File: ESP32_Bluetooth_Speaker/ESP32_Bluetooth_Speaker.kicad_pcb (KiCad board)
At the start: 2 copper layers, 88.9 x 63.5 mm, 51 parts, among them J2 POWER INPUT, Q1 MMBT3904, Q2 MMBT3904, SW1 PAUSE, SW2 PREV, SW3 NEXT, SW4 V+, SW5 V-, SW6 RESET, U1 FT231XS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

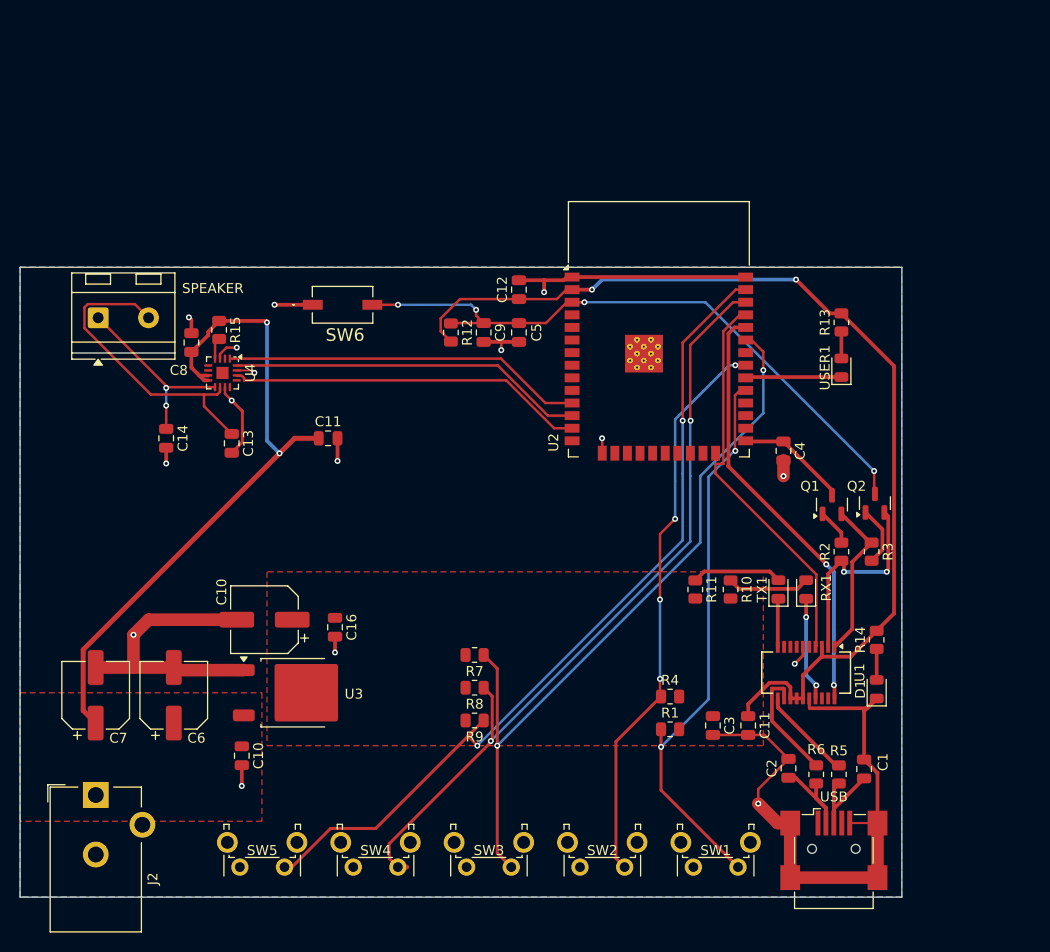
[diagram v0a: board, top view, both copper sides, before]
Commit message: Added CAD assembly and surface mount PCB initial rev
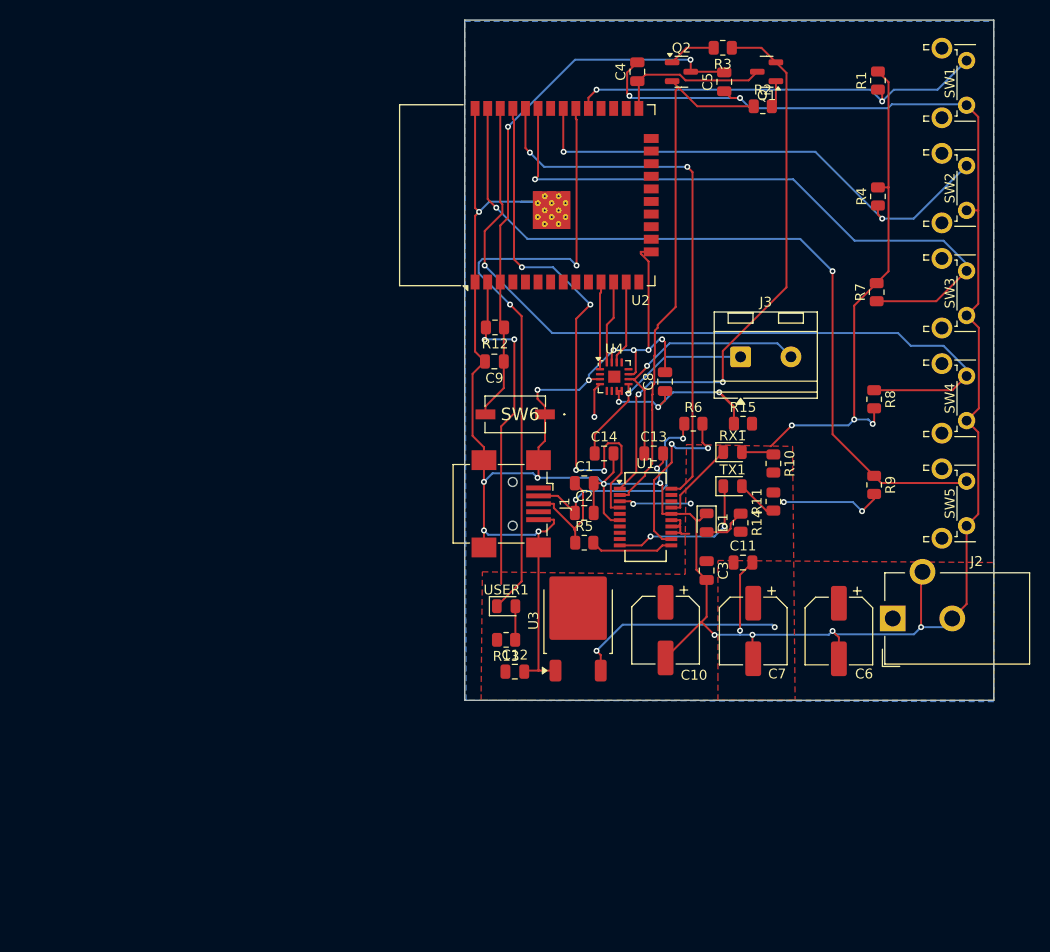
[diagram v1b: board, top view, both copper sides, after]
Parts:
- removed the C10 at (93.5, 141.5)
- removed the C10 at (95.8, 127.8)
- removed the C11 at (102.2, 109.5)
- removed the C11 at (144.5, 138.4)
- removed C16: 0.1uF, Capacitor_SMD:C_0805_2012Metric
- removed SPEAKER: SPEAKER, TerminalBlock_RND:TerminalBlock_RND_205-00232_1x02_P5.08mm_Horizontal
- removed USB: USB_B_Mini, Connector_USB:USB_Mini-B_Wuerth_65100516121_Horizontal
- added C10: 47uF, Capacitor_SMD:CP_Elec_6.3x5.4, F.Cu at (136.2, 128.8)
- added C11: 0.1uF, Capacitor_SMD:C_0805_2012Metric, F.Cu at (144.0, 122.0)
- added J1: USB_B_Mini, Connector_USB:USB_Mini-B_Wuerth_65100516121_Horizontal, F.Cu at (120.8, 116.1)
- added J3: SPEAKER, TerminalBlock_RND:TerminalBlock_RND_205-00232_1x02_P5.08mm_Horizontal, F.Cu at (143.8, 101.3)
- moved SW1 84.5 mm to (166.5, 71.4), turned to -90 degrees
- moved J2 82.3 mm to (159.1, 127.6), turned to 90 degrees
- moved SW5 79.0 mm to (166.5, 113.8), turned to -90 degrees
- moved SW2 78.7 mm to (166.5, 82.0), turned to -90 degrees
- moved SW4 75.8 mm to (166.5, 103.2), turned to -90 degrees
- moved SW3 75.6 mm to (166.5, 92.6), turned to -90 degrees
- moved R1 68.7 mm to (157.6, 73.4), turned to 90 degrees
- moved C6 67.4 mm to (153.7, 128.9), turned to -90 degrees
- moved C7 66.6 mm to (145.0, 128.9), turned to -90 degrees
- moved R4 54.6 mm to (157.6, 85.1), turned to 90 degrees
- moved R7 54.6 mm to (157.5, 94.7), turned to 90 degrees
- moved R15 53.7 mm to (144.0, 108.0), turned to 0 degrees
- moved R3 53.0 mm to (142.0, 70.1), turned to 180 degrees
- moved R8 49.7 mm to (157.2, 105.5), turned to -90 degrees
- moved C8 47.9 mm to (136.1, 103.8)
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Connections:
- U2 pad 5: ~{RTCINT} -> unconnected-(U2-SENSOR_VN-Pad5)
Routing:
- net GND: track 151.2 -> 346.1 mm, vias 16 -> 21
- net Net-(U2-IO18): track 9.68 -> 63.6 mm, vias 0 -> 2
- net DTR: track 16.3 -> 60.5 mm, vias 0 -> 2
- net RTS: track 21.0 -> 53.3 mm, vias 2 -> 0
- net LRCLK: track 36.1 -> 8.50 mm
- net DIN: track 36.3 -> 8.84 mm
- net BCLK: track 35.9 -> 8.39 mm
- net +5V: track 68.1 -> 47.9 mm, vias 2 -> 5
- net RXD: track 39.8 -> 57.0 mm, vias 0 -> 4
- net Net-(J1-D-): track 9.43 -> 23.5 mm, vias 0 -> 2
- net PB1: track 57.0 -> 43.1 mm
- net TXD: track 43.2 -> 55.2 mm
- net Net-(TX1-K): track 4.87 -> 15.5 mm, vias 0 -> 2
- net PB3: track 75.6 -> 65.4 mm, vias 2 -> 1
- net EN: track 65.3 -> 56.1 mm, vias 4 -> 2
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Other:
- board size 88.9 x 63.5 mm -> 53.3 x 68.6 mm
